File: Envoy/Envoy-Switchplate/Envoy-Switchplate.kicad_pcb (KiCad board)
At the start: 2 copper layers, 95.4 x 95.4 mm, 32 parts

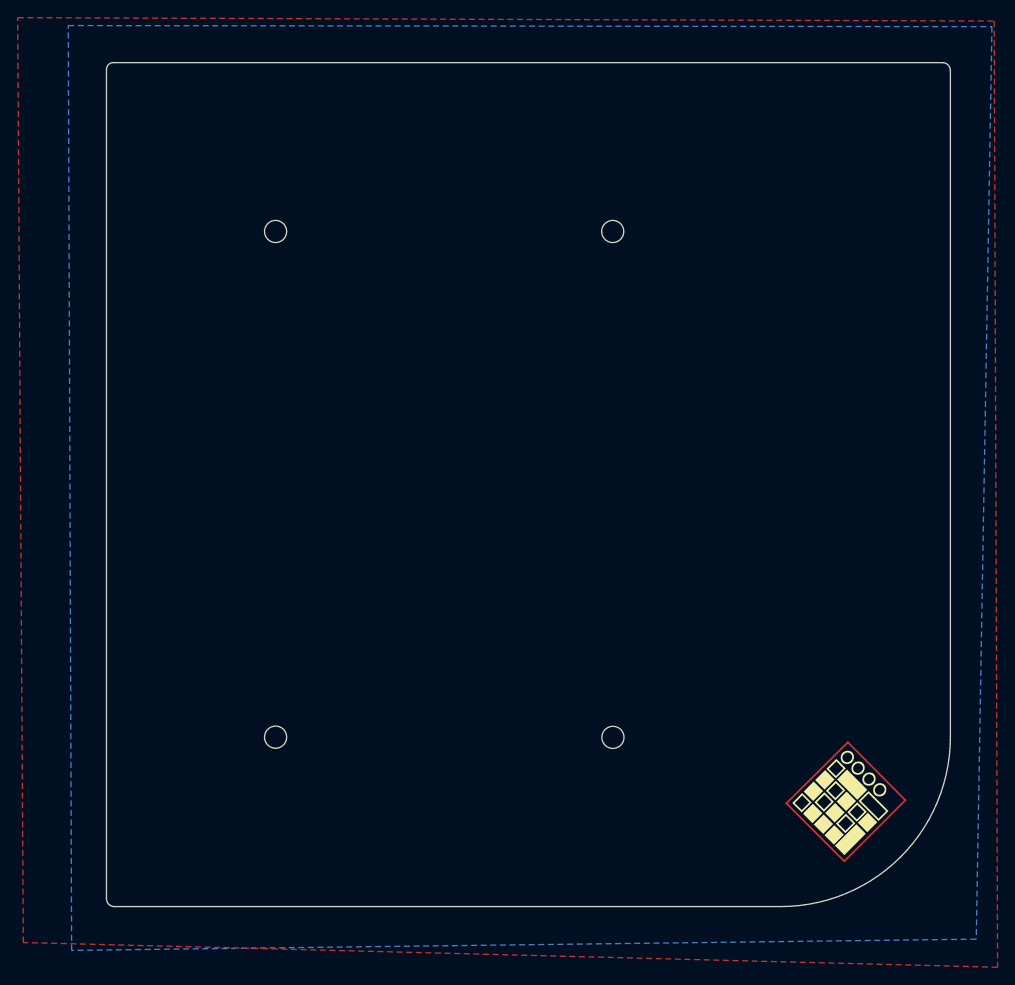
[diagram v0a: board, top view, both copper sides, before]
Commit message: Fix switchplate cutout sizes
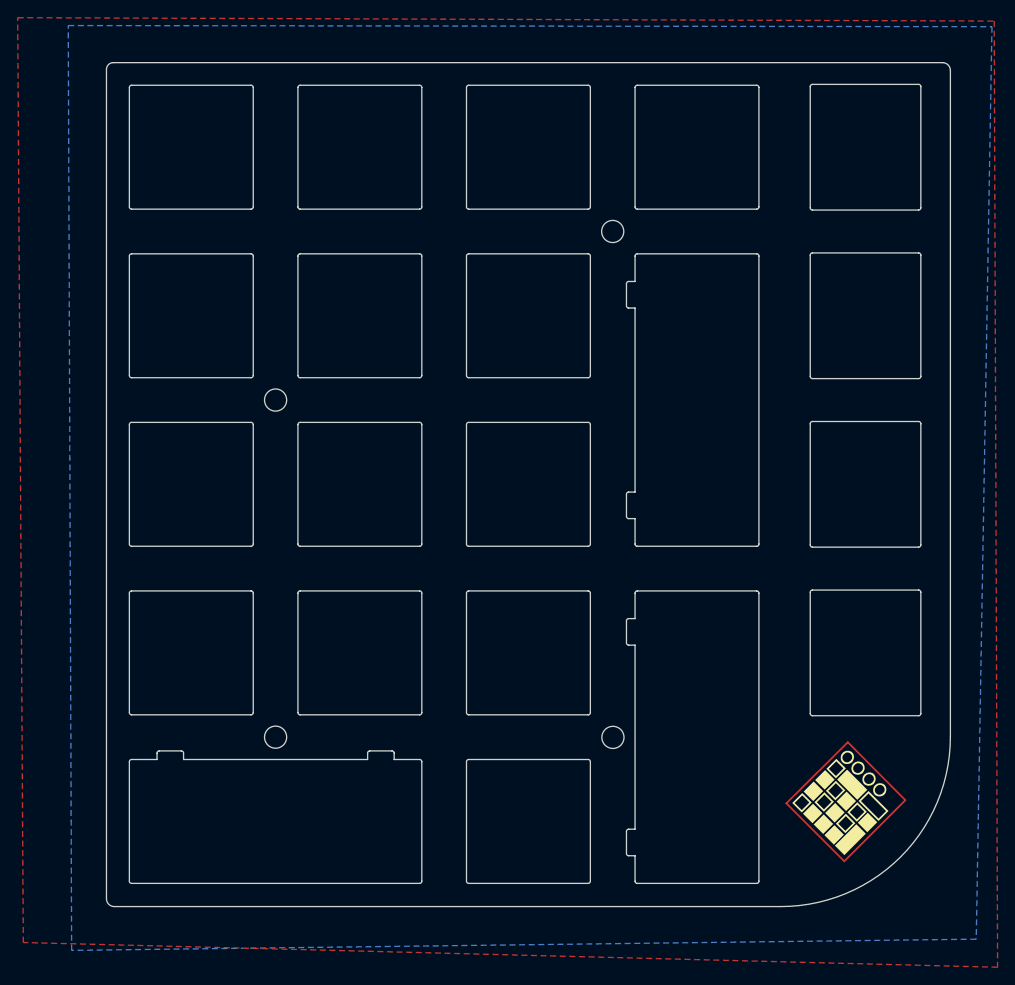
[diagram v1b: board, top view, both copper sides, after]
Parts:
- removed MX12, MX16, MX17, MX18, MX20, MX8: MX-NoLED, Envoy:MX_Switch_Cutout_Square
- MX16-2u1, MX8-2u1: footprint Envoy:MX_Switch_Cutout-2u_with_stabilizer_nibbles -> Envoy:MX_Switch_Cutout-Combo-2u_2x1u
- MX17-2u1: footprint Envoy:MX_Switch_Cutout-2u_with_reversed_stabilizer_nibbles -> Envoy:MX_Switch_Cutout-Combo-2u_2x1u
- moved H1 19.0 mm to (112.0, 104.4)
- turned MX17-2u1 to 180 degrees

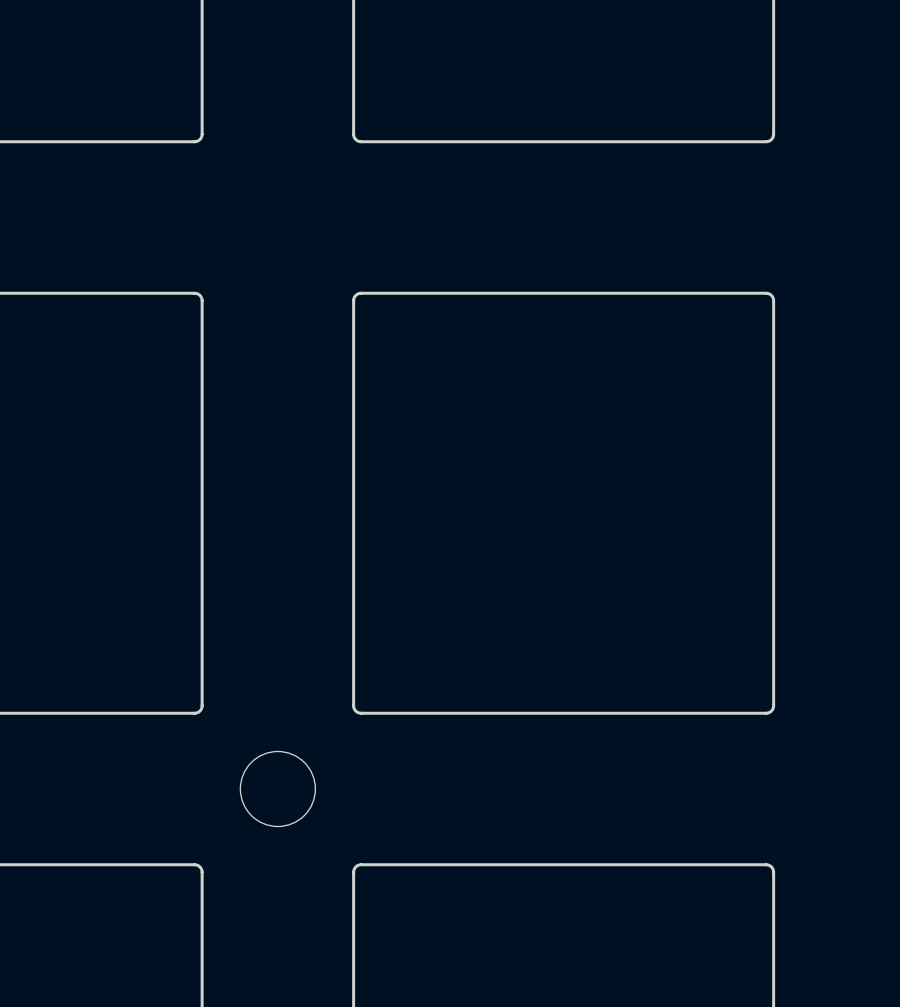
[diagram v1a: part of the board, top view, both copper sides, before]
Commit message: Move standoff and bumper positioning to make the backplate work easier
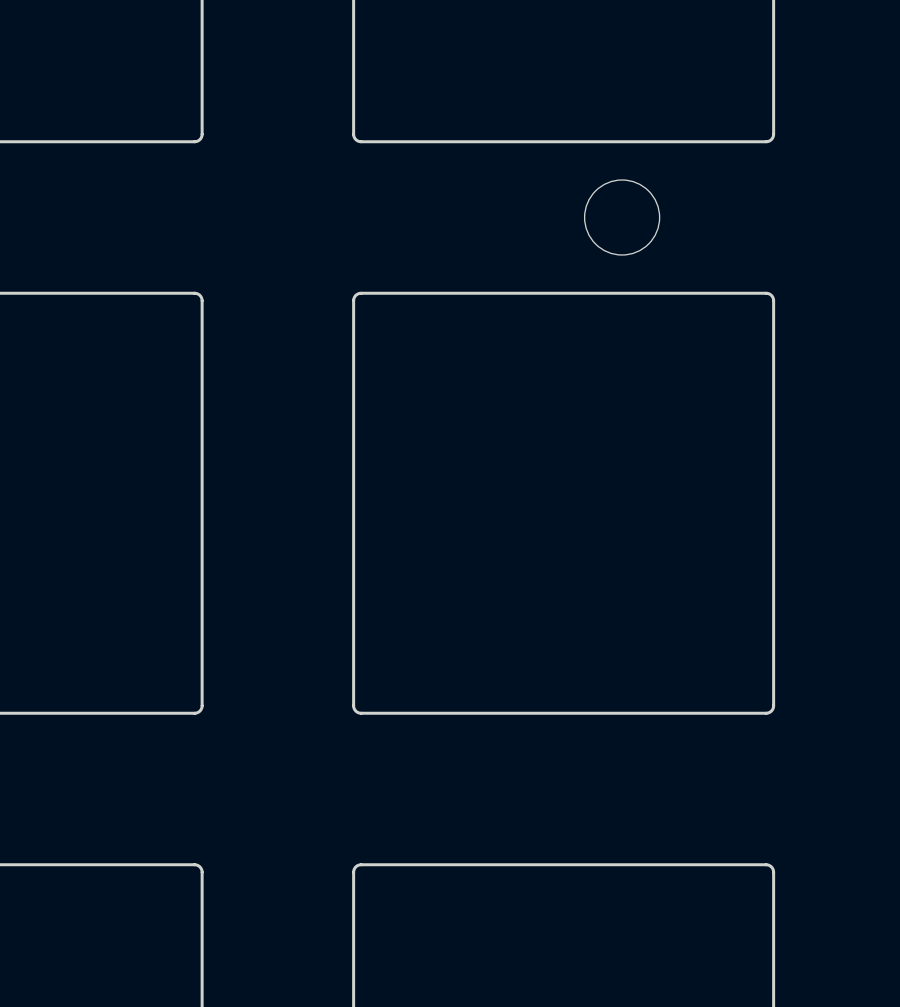
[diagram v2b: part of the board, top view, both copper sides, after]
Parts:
- moved H1 22.2 mm to (123.4, 85.4)
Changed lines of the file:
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@@
   )
   (footprint "MountingHole:MountingHole_2.5mm" (layer "F.Cu")
-    (at 111.9505 104.42575)
+    (at 123.425 85.37575)
     (descr "Mounting Hole 2.5mm, no annular")
     (tags "mounting hole 2.5mm no annular")
